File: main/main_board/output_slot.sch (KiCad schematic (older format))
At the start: 1 part, among them P1 my_pcie_8x

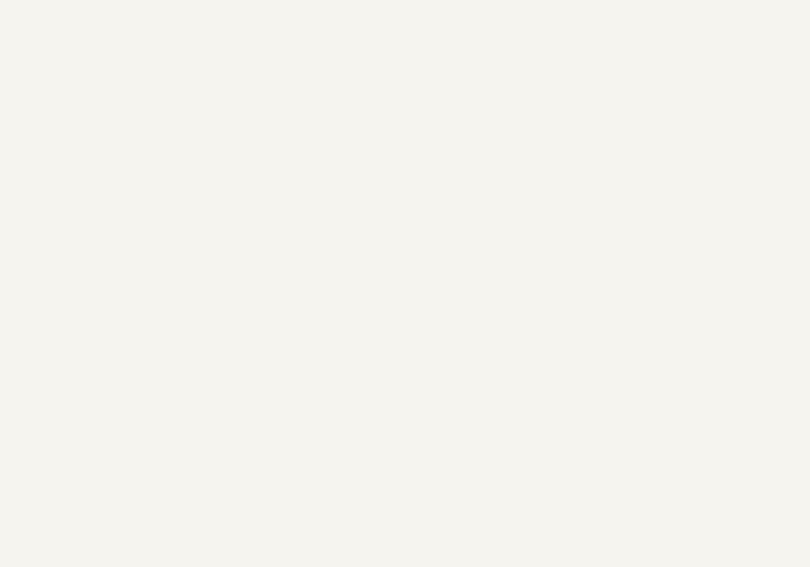
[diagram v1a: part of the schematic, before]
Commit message: A bunch of thinking about RFI and ESD, and some testing.  Mostly reflected in notebook.txt. Also another more explicit round of consideration of box-level grounding and power distribution, because this affects the power conditioning on the main board.  Power nets on the main board are mostly captured.  I added supply decoupling at each plugin slot.
in_filter.sxsch: added simulation of ESD, use vendor models for TVS diode and ferrite.

power_budget.xlsx: get rid of sheets for the input boards not implemented.  Add sheet for
the main board and carry over data from the input board sheet.
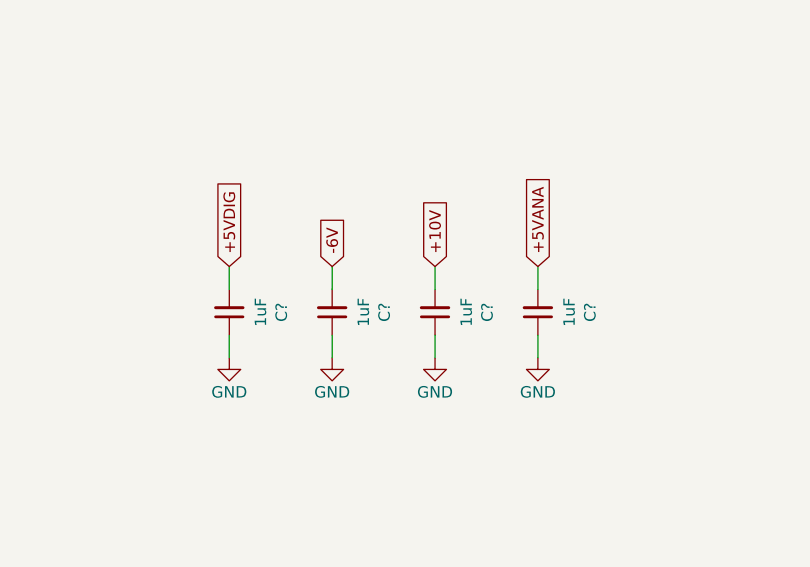
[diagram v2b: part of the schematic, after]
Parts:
- added C? (x4): 1uF, Capacitor_SMD:C_0805_2012Metric, symbol Device:C_Small
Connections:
- net +10V: now also C?.2
- net +5VANA: now also C?.2
- net +5VDIG: now also C?.2
- net -6V: now also C?.2
- net GND: now also C?.1, C?.1, C?.1, C?.1
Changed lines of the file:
@@
 Text Notes 7450 2450 1    50   ~ 0
 -- High speed LDVS digital --
+Text GLabel 8150 5200 1    50   Input ~ 0
+-6V
+Text GLabel 8600 5200 1    50   Input ~ 0
++10V
+Text GLabel 9050 5200 1    50   Input ~ 0
++5VANA
+Text GLabel 7700 5200 1    50   Input ~ 0
++5VDIG
+$Comp
+L Device:C_Small C?
+U 1 1 5EE014BD
+P 7700 5400
+AR Path="/5DFF6C0D/5EE014BD" Ref="C?"  Part="1"
+AR Path="/5E1D6729/5E1DA2AA/5EE014BD" Ref="C?"  Part="1"
+AR Path="/5E2EB92B/5EE014BD" Ref="C?"  Part="1"
+AR Path="/5E51E83D/5EE014BD" Ref="C?"  Part="1"
+AR Path="/5E624B3C/5E51E83D/5EE014BD" Ref="C?"  Part="1"
+AR Path="/5E525F2C/5EE014BD" Ref="C?"  Part="1"
+AR Path="/5E525FC9/5EE014BD" Ref="C?"  Part="1"
+AR Path="/5E525FFE/5EBAAEAF/5EE014BD" Ref="C?"  Part="1"
+F 0 "C?" V 7471 5400 50  0000 C CNN
+F 1 "1uF" V 7562 5400 50  0000 C CNN
+F 2 "Capacitor_SMD:C_0805_2012Metric" H 7700 5400 50  0001 C CNN
+F 3 "https://media.digikey.com/pdf/Data%20Sheets/Samsung%20PDFs/CL_Series_MLCC_ds.pdf" H 7700 5400 50  0001 C CNN
+F 4 "CAP CER 1UF 16V X7R 0805 " H 7700 5400 50  0001 C CNN "Description"
+F 5 "1276-6471-1-ND" H 7700 5400 50  0001 C CNN "Digikey"
+F 6 "CL21B105KOFNNNG" H 7700 5400 50  0001 C CNN "MPN"
+F 7 "27" H 7700 5400 50  0001 C CNN "DK line"
+	1    7700 5400
+	-1   0    0    1
+$EndComp
+$Comp
+L power:GND #PWR?
+U 1 1 5EE014C3
+P 7700 5600
+AR Path="/5E525F2C/5E59D3A2/5EE014C3" Ref="#PWR?"  Part="1"
+AR Path="/5E525F2C/5E76A42A/5EE014C3" Ref="#PWR?"  Part="1"
+AR Path="/5E525F2C/5E76E218/5EE014C3" Ref="#PWR?"  Part="1"
+AR Path="/5E525F2C/5E7721D1/5EE014C3" Ref="#PWR?"  Part="1"
+AR Path="/5E525FFE/5EBAAEAF/5EE014C3" Ref="#PWR?"  Part="1"
+AR Path="/5E525FFE/5EBAAF7D/5EE014C3" Ref="#PWR?"  Part="1"
+AR Path="/5E525FFE/5EBAAF8F/5EE014C3" Ref="#PWR?"  Part="1"
+AR Path="/5E525FFE/5EBAAFA1/5EE014C3" Ref="#PWR?"  Part="1"
+F 0 "#PWR?" H 7700 5350 50  0001 C CNN
+F 1 "GND" H 7700 5450 50  0000 C CNN
+F 2 "" H 7700 5600 50  0001 C CNN
+F 3 "" H 7700 5600 50  0001 C CNN
+	1    7700 5600
+	1    0    0    -1
+$EndComp
+Wire Wire Line
+	7700 5200 7700 5300
+Wire Wire Line
+	7700 5500 7700 5600
+$Comp
+L Device:C_Small C?
+U 1 1 5EE014CF
+P 8150 5400
+AR Path="/5DFF6C0D/5EE014CF" Ref="C?"  Part="1"
+AR Path="/5E1D6729/5E1DA2AA/5EE014CF" Ref="C?"  Part="1"
+AR Path="/5E2EB92B/5EE014CF" Ref="C?"  Part="1"
+AR Path="/5E51E83D/5EE014CF" Ref="C?"  Part="1"
+AR Path="/5E624B3C/5E51E83D/5EE014CF" Ref="C?"  Part="1"
+AR Path="/5E525F2C/5EE014CF" Ref="C?"  Part="1"
+AR Path="/5E525FC9/5EE014CF" Ref="C?"  Part="1"
+AR Path="/5E525FFE/5EBAAEAF/5EE014CF" Ref="C?"  Part="1"
+F 0 "C?" V 7921 5400 50  0000 C CNN
+F 1 "1uF" V 8012 5400 50  0000 C CNN
+F 2 "Capacitor_SMD:C_0805_2012Metric" H 8150 5400 50  0001 C CNN
+F 3 "https://media.digikey.com/pdf/Data%20Sheets/Samsung%20PDFs/CL_Series_MLCC_ds.pdf" H 8150 5400 50  0001 C CNN
+F 4 "CAP CER 1UF 16V X7R 0805 " H 8150 5400 50  0001 C CNN "Description"
+F 5 "1276-6471-1-ND" H 8150 5400 50  0001 C CNN "Digikey"
+F 6 "CL21B105KOFNNNG" H 8150 5400 50  0001 C CNN "MPN"
+F 7 "27" H 8150 5400 50  0001 C CNN "DK line"
+	1    8150 5400
+	-1   0    0    1
+$EndComp
+$Comp
+L power:GND #PWR?
+U 1 1 5EE014D5
+P 8150 5600
+AR Path="/5E525F2C/5E59D3A2/5EE014D5" Ref="#PWR?"  Part="1"
+AR Path="/5E525F2C/5E76A42A/5EE014D5" Ref="#PWR?"  Part="1"
+AR Path="/5E525F2C/5E76E218/5EE014D5" Ref="#PWR?"  Part="1"
+AR Path="/5E525F2C/5E7721D1/5EE014D5" Ref="#PWR?"  Part="1"
+AR Path="/5E525FFE/5EBAAEAF/5EE014D5" Ref="#PWR?"  Part="1"
+AR Path="/5E525FFE/5EBAAF7D/5EE014D5" Ref="#PWR?"  Part="1"
+AR Path="/5E525FFE/5EBAAF8F/5EE014D5" Ref="#PWR?"  Part="1"
+AR Path="/5E525FFE/5EBAAFA1/5EE014D5" Ref="#PWR?"  Part="1"
+F 0 "#PWR?" H 8150 5350 50  0001 C CNN
+F 1 "GND" H 8150 5450 50  0000 C CNN
+F 2 "" H 8150 5600 50  0001 C CNN
+F 3 "" H 8150 5600 50  0001 C CNN
+	1    8150 5600
+	1    0    0    -1
+$EndComp
+Wire Wire Line
+	8150 5200 8150 5300
+Wire Wire Line
+	8150 5500 8150 5600
+$Comp
+L Device:C_Small C?
+U 1 1 5EE014E1
+P 8600 5400
+AR Path="/5DFF6C0D/5EE014E1" Ref="C?"  Part="1"
+AR Path="/5E1D6729/5E1DA2AA/5EE014E1" Ref="C?"  Part="1"
+AR Path="/5E2EB92B/5EE014E1" Ref="C?"  Part="1"
+AR Path="/5E51E83D/5EE014E1" Ref="C?"  Part="1"
+AR Path="/5E624B3C/5E51E83D/5EE014E1" Ref="C?"  Part="1"
+AR Path="/5E525F2C/5EE014E1" Ref="C?"  Part="1"
+AR Path="/5E525FC9/5EE014E1" Ref="C?"  Part="1"
+AR Path="/5E525FFE/5EBAAEAF/5EE014E1" Ref="C?"  Part="1"
+F 0 "C?" V 8371 5400 50  0000 C CNN
+F 1 "1uF" V 8462 5400 50  0000 C CNN
+F 2 "Capacitor_SMD:C_0805_2012Metric" H 8600 5400 50  0001 C CNN
+F 3 "https://media.digikey.com/pdf/Data%20Sheets/Samsung%20PDFs/CL_Series_MLCC_ds.pdf" H 8600 5400 50  0001 C CNN
+F 4 "CAP CER 1UF 16V X7R 0805 " H 8600 5400 50  0001 C CNN "Description"
+F 5 "1276-6471-1-ND" H 8600 5400 50  0001 C CNN "Digikey"
+F 6 "CL21B105KOFNNNG" H 8600 5400 50  0001 C CNN "MPN"
+F 7 "27" H 8600 5400 50  0001 C CNN "DK line"
+	1    8600 5400
+	-1   0    0    1
+$EndComp
+$Comp
+L power:GND #PWR?
+U 1 1 5EE014E7
+P 8600 5600
+AR Path="/5E525F2C/5E59D3A2/5EE014E7" Ref="#PWR?"  Part="1"
+AR Path="/5E525F2C/5E76A42A/5EE014E7" Ref="#PWR?"  Part="1"
+AR Path="/5E525F2C/5E76E218/5EE014E7" Ref="#PWR?"  Part="1"
+AR Path="/5E525F2C/5E7721D1/5EE014E7" Ref="#PWR?"  Part="1"
+AR Path="/5E525FFE/5EBAAEAF/5EE014E7" Ref="#PWR?"  Part="1"
+AR Path="/5E525FFE/5EBAAF7D/5EE014E7" Ref="#PWR?"  Part="1"
+AR Path="/5E525FFE/5EBAAF8F/5EE014E7" Ref="#PWR?"  Part="1"
+AR Path="/5E525FFE/5EBAAFA1/5EE014E7" Ref="#PWR?"  Part="1"
+F 0 "#PWR?" H 8600 5350 50  0001 C CNN
+F 1 "GND" H 8600 5450 50  0000 C CNN
+F 2 "" H 8600 5600 50  0001 C CNN
+F 3 "" H 8600 5600 50  0001 C CNN
+	1    8600 5600
+	1    0    0    -1
+$EndComp
+Wire Wire Line
+	8600 5200 8600 5300
+Wire Wire Line
+	8600 5500 8600 5600
+$Comp
+L Device:C_Small C?
+U 1 1 5EE014F3
+P 9050 5400
+AR Path="/5DFF6C0D/5EE014F3" Ref="C?"  Part="1"
+AR Path="/5E1D6729/5E1DA2AA/5EE014F3" Ref="C?"  Part="1"
+AR Path="/5E2EB92B/5EE014F3" Ref="C?"  Part="1"
+AR Path="/5E51E83D/5EE014F3" Ref="C?"  Part="1"
+AR Path="/5E624B3C/5E51E83D/5EE014F3" Ref="C?"  Part="1"
+AR Path="/5E525F2C/5EE014F3" Ref="C?"  Part="1"
+AR Path="/5E525FC9/5EE014F3" Ref="C?"  Part="1"
+AR Path="/5E525FFE/5EBAAEAF/5EE014F3" Ref="C?"  Part="1"
+F 0 "C?" V 8821 5400 50  0000 C CNN
+F 1 "1uF" V 8912 5400 50  0000 C CNN
+F 2 "Capacitor_SMD:C_0805_2012Metric" H 9050 5400 50  0001 C CNN
+F 3 "https://media.digikey.com/pdf/Data%20Sheets/Samsung%20PDFs/CL_Series_MLCC_ds.pdf" H 9050 5400 50  0001 C CNN
+F 4 "CAP CER 1UF 16V X7R 0805 " H 9050 5400 50  0001 C CNN "Description"
+F 5 "1276-6471-1-ND" H 9050 5400 50  0001 C CNN "Digikey"
+F 6 "CL21B105KOFNNNG" H 9050 5400 50  0001 C CNN "MPN"
+F 7 "27" H 9050 5400 50  0001 C CNN "DK line"
+	1    9050 5400
+	-1   0    0    1
+$EndComp
+$Comp
+L power:GND #PWR?
+U 1 1 5EE014F9
+P 9050 5600
+AR Path="/5E525F2C/5E59D3A2/5EE014F9" Ref="#PWR?"  Part="1"
+AR Path="/5E525F2C/5E76A42A/5EE014F9" Ref="#PWR?"  Part="1"
+AR Path="/5E525F2C/5E76E218/5EE014F9" Ref="#PWR?"  Part="1"
+AR Path="/5E525F2C/5E7721D1/5EE014F9" Ref="#PWR?"  Part="1"
+AR Path="/5E525FFE/5EBAAEAF/5EE014F9" Ref="#PWR?"  Part="1"
+AR Path="/5E525FFE/5EBAAF7D/5EE014F9" Ref="#PWR?"  Part="1"
+AR Path="/5E525FFE/5EBAAF8F/5EE014F9" Ref="#PWR?"  Part="1"
+AR Path="/5E525FFE/5EBAAFA1/5EE014F9" Ref="#PWR?"  Part="1"
+F 0 "#PWR?" H 9050 5350 50  0001 C CNN
+F 1 "GND" H 9050 5450 50  0000 C CNN
+F 2 "" H 9050 5600 50  0001 C CNN
+F 3 "" H 9050 5600 50  0001 C CNN
+	1    9050 5600
+	1    0    0    -1
+$EndComp
+Wire Wire Line
+	9050 5200 9050 5300
+Wire Wire Line
+	9050 5500 9050 5600
 $EndSCHEMATC

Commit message: Diffs mainly due to first annotation of some new components.  Also changes on power.sch, added TVS and some caps.
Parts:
- gave numbers to parts that had none: 4
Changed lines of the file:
@@
 AR Path="/5E525FC9/5EE014BD" Ref="C?"  Part="1"
 AR Path="/5E525FFE/5EBAAEAF/5EE014BD" Ref="C?"  Part="1"
-F 0 "C?" V 7471 5400 50  0000 C CNN
+AR Path="/5EC15224/5EE014BD" Ref="C40"  Part="1"
+F 0 "C40" V 7471 5400 50  0000 C CNN
 F 1 "1uF" V 7562 5400 50  0000 C CNN
 F 2 "Capacitor_SMD:C_0805_2012Metric" H 7700 5400 50  0001 C CNN
@@
 AR Path="/5E525FFE/5EBAAF8F/5EE014C3" Ref="#PWR?"  Part="1"
 AR Path="/5E525FFE/5EBAAFA1/5EE014C3" Ref="#PWR?"  Part="1"
-F 0 "#PWR?" H 7700 5350 50  0001 C CNN
+AR Path="/5EC15224/5EE014C3" Ref="#PWR037"  Part="1"
+F 0 "#PWR037" H 7700 5350 50  0001 C CNN
 F 1 "GND" H 7700 5450 50  0000 C CNN
 F 2 "" H 7700 5600 50  0001 C CNN
@@
 AR Path="/5E525FC9/5EE014CF" Ref="C?"  Part="1"
 AR Path="/5E525FFE/5EBAAEAF/5EE014CF" Ref="C?"  Part="1"
-F 0 "C?" V 7921 5400 50  0000 C CNN
+AR Path="/5EC15224/5EE014CF" Ref="C43"  Part="1"
+F 0 "C43" V 7921 5400 50  0000 C CNN
 F 1 "1uF" V 8012 5400 50  0000 C CNN
 F 2 "Capacitor_SMD:C_0805_2012Metric" H 8150 5400 50  0001 C CNN
@@
 AR Path="/5E525FFE/5EBAAF8F/5EE014D5" Ref="#PWR?"  Part="1"
 AR Path="/5E525FFE/5EBAAFA1/5EE014D5" Ref="#PWR?"  Part="1"
-F 0 "#PWR?" H 8150 5350 50  0001 C CNN
+AR Path="/5EC15224/5EE014D5" Ref="#PWR038"  Part="1"
+F 0 "#PWR038" H 8150 5350 50  0001 C CNN
 F 1 "GND" H 8150 5450 50  0000 C CNN
 F 2 "" H 8150 5600 50  0001 C CNN
@@
 AR Path="/5E525FC9/5EE014E1" Ref="C?"  Part="1"
 AR Path="/5E525FFE/5EBAAEAF/5EE014E1" Ref="C?"  Part="1"
-F 0 "C?" V 8371 5400 50  0000 C CNN
+AR Path="/5EC15224/5EE014E1" Ref="C45"  Part="1"
+F 0 "C45" V 8371 5400 50  0000 C CNN
 F 1 "1uF" V 8462 5400 50  0000 C CNN
 F 2 "Capacitor_SMD:C_0805_2012Metric" H 8600 5400 50  0001 C CNN
@@
 AR Path="/5E525FFE/5EBAAF8F/5EE014E7" Ref="#PWR?"  Part="1"
 AR Path="/5E525FFE/5EBAAFA1/5EE014E7" Ref="#PWR?"  Part="1"
-F 0 "#PWR?" H 8600 5350 50  0001 C CNN
+AR Path="/5EC15224/5EE014E7" Ref="#PWR039"  Part="1"
+F 0 "#PWR039" H 8600 5350 50  0001 C CNN
 F 1 "GND" H 8600 5450 50  0000 C CNN
 F 2 "" H 8600 5600 50  0001 C CNN
@@
 AR Path="/5E525FC9/5EE014F3" Ref="C?"  Part="1"
 AR Path="/5E525FFE/5EBAAEAF/5EE014F3" Ref="C?"  Part="1"
-F 0 "C?" V 8821 5400 50  0000 C CNN
+AR Path="/5EC15224/5EE014F3" Ref="C53"  Part="1"
+F 0 "C53" V 8821 5400 50  0000 C CNN
 F 1 "1uF" V 8912 5400 50  0000 C CNN
 F 2 "Capacitor_SMD:C_0805_2012Metric" H 9050 5400 50  0001 C CNN
@@
 AR Path="/5E525FFE/5EBAAF8F/5EE014F9" Ref="#PWR?"  Part="1"
 AR Path="/5E525FFE/5EBAAFA1/5EE014F9" Ref="#PWR?"  Part="1"
-F 0 "#PWR?" H 9050 5350 50  0001 C CNN
+AR Path="/5EC15224/5EE014F9" Ref="#PWR040"  Part="1"
+F 0 "#PWR040" H 9050 5350 50  0001 C CNN
 F 1 "GND" H 9050 5450 50  0000 C CNN
 F 2 "" H 9050 5600 50  0001 C CNN

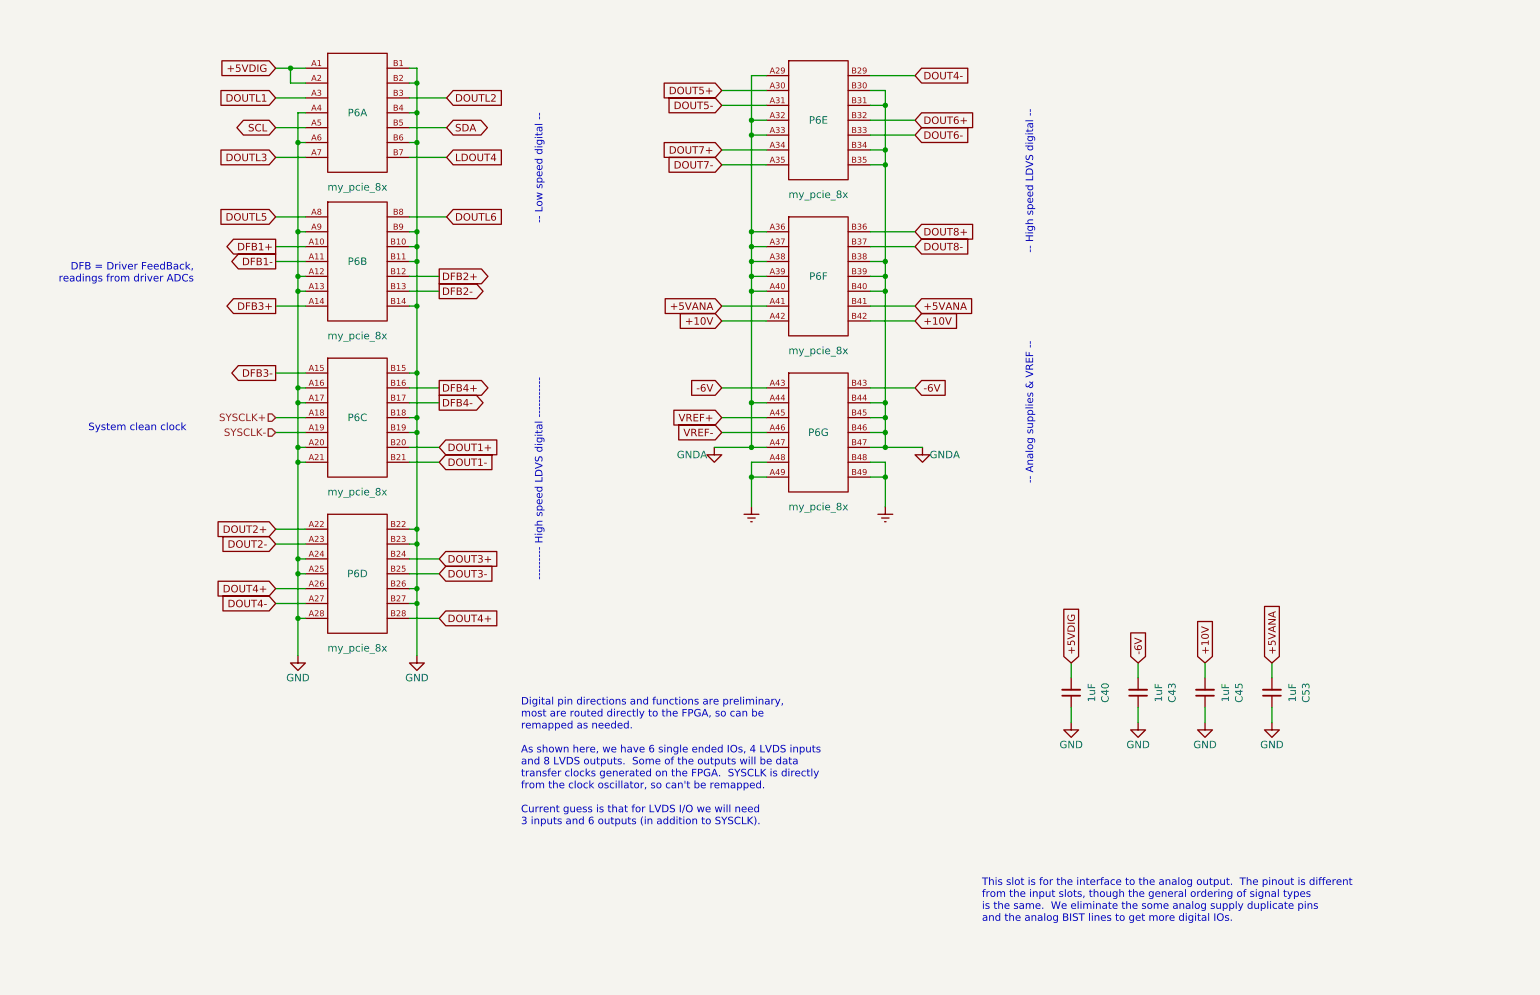
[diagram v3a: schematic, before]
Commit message: Mostly work on hooking in the Microzed using kipart symbols and a footprint. Also added 2.5V VCCIO regulator.
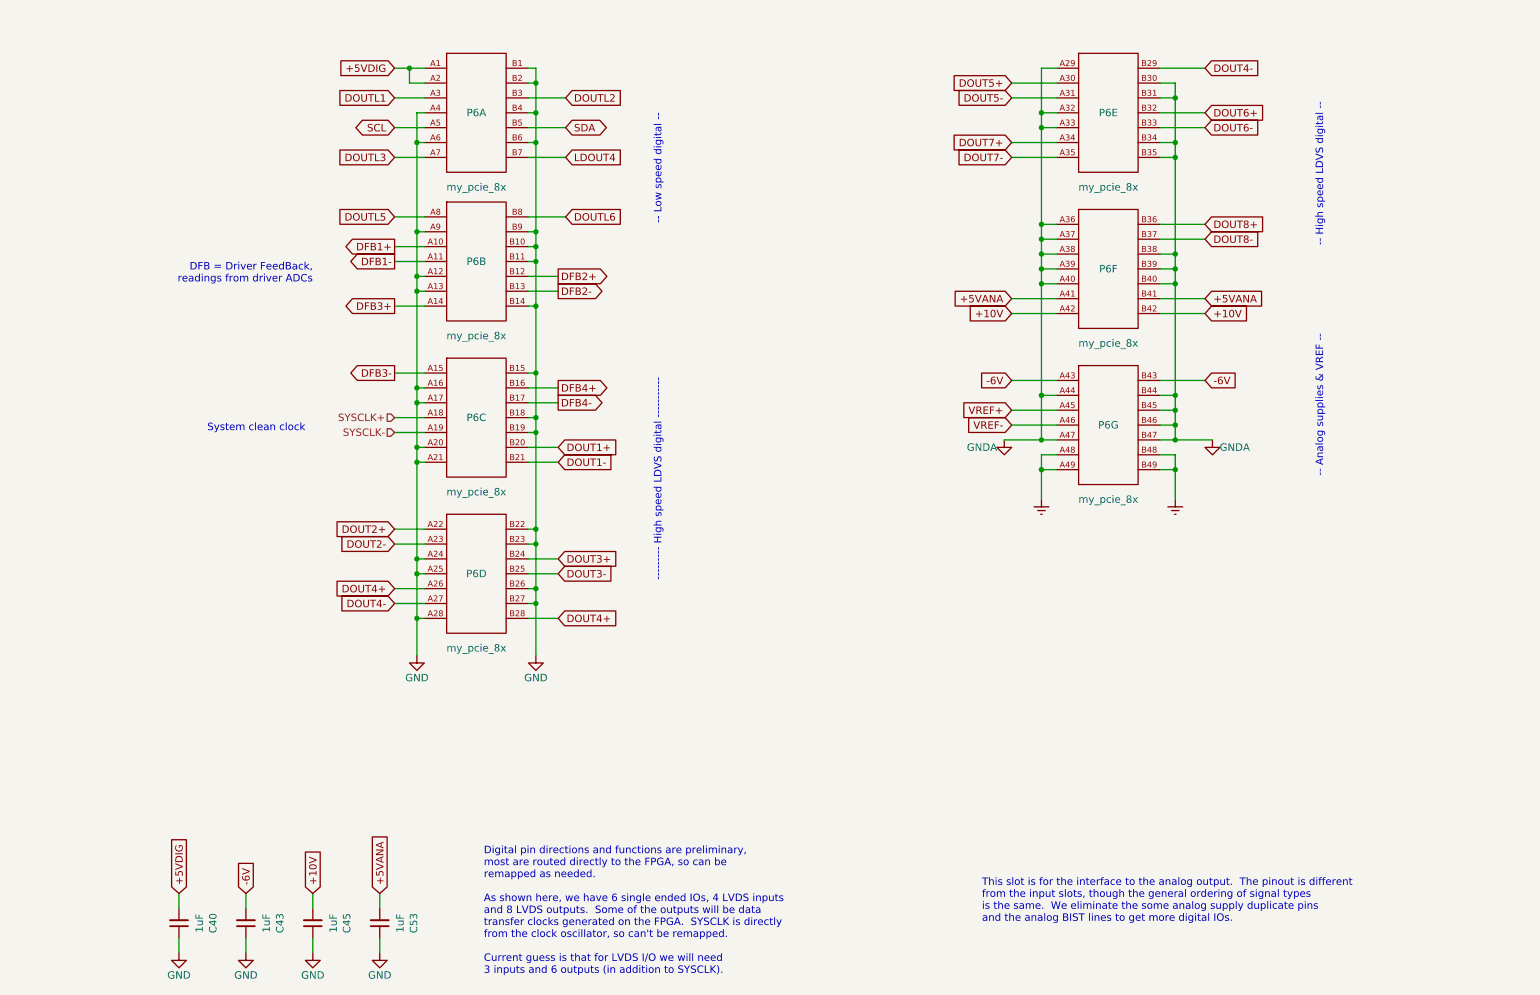
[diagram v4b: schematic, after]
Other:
- moved on the sheet: C40, C43, C45, C53, P6A, P6B, P6C, P6D, P6E, P6F, P6G
